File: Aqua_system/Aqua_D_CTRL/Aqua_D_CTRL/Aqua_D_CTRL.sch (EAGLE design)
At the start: 233 parts, among them IC1 SN65HVD3082EDR, IC2 CSTNE8M00G520000R0, IC3 LT6106CS5#TRPBF, IC4 LT6106CS5#TRPBF, IC5 TPS54202DDCR, IC6 LD1117S33TR, IC8 LM317AEMP, J1 ESP32-PICO-KIT, K1 KB20C06A, K2 KB20C06A, Q1 DMP6185SEQ-13, Q10 BC817, Q11 2N7002, Q12 DMP6185SEQ-13, Q13 2N7002, Q14 DMP6185SEQ-13, Q15 2N7002, Q16 DMP6185SEQ-13, Q17 BC817, Q18 BC817, Q19 BC817, Q2 2N7002, Q20 BC817, Q21 BC817, Q22 BC817, Q23 BC817, Q3 DMP6185SEQ-13, Q4 2N7002, Q5 DMP6185SEQ-13, Q6 DMP6185SEQ-13, Q7 2N7002, Q8 DMP6185SEQ-13, Q9 2N7002, SW1 L101011MS02Q, U2 RENESAS_R7FA6M5BG3CFBLQFP_144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, X1 B2B-XH-AM(LF)(SN), X10 726386-2TE_726386-2, X11 282834-2, X12 RJ45-8L-B, X13 MICROMATCH-16, X14 RJ45-8L-B, X2 WF2549-2WS05S0B01, X3 282834-3, X4 282834-3, X5 726386-2TE_726386-2, X6 726386-2TE_726386-2, X7 726386-2TE_726386-2, X8 726386-2TE_726386-2, X9 726386-2TE_726386-2

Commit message: HW00.00 Ongoing
Layout ongoing
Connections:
- removed net N$90: C67.2
- net AI_24V0: now also U2B.P502
- net AI_I_SENSE_CONDUTIV_SENSOR: now also U2B.P503
- net AI_I_SENSE_PH_SENSOR: now also U2B.P500
- net AI_V_CONDUCTIV_SENSOR: now also U2B.P504
- net AI_V_PH_SENSOR: now also U2B.P501
- net GND: now also U2B.AVSS0, U2B.VREFL0, U2B.VSS, U2B.VSS_5, U2B.VSS_6
- net VCC: now also C67.2, U2B.AVCC0, U2B.VCC, U2B.VCC_5, U2B.VCC_6, U2B.VREFH0
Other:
- moved on the sheet: C60, C61, C62, C63, C64, C65, C66, C67, C68

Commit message: HW00.00 Layout Ongoing
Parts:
- removed R95: 2.2K 1%, Labops_Lib_AH:R_0603
- C67: value 100nF/50V -> 1unF/50V
- U2: value RENESAS_R7FA6M5BG3CFBLQFP_144_20X20_REN-M -> R7FA6M5BG3CFBLQFP_144_20X20_REN-M; device 3D_MIG_Controller:RENESAS_R7FA6M5BG3CFBLQFP_144_20X20_REN-M -> Labops_Lib_AH:R7FA6M5BG3CFBLQFP_144_20X20_REN-M
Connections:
- removed net N$59: R95.2
- net GND: now also U2B.VREFL; no longer R95.1, U2B.VREFL0
- net VCC: now also U2B.VREFH; no longer U2B.VREFH0
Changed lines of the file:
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@@
 <part name="C50" library="Labops_Lib_AH" deviceset="C_0603" device="" value="100nF/50V"/>
 <part name="GND70" library="3D_MIG_Controller" deviceset="GND" device=""/>
-<part name="R95" library="Labops_Lib_AH" deviceset="R_0603" device="" value="2.2K 1%"/>
-<part name="GND71" library="3D_MIG_Controller" deviceset="GND" device=""/>
 <part name="GND72" library="3D_MIG_Controller" deviceset="GND" device=""/>
 <part name="C51" library="Labops_Lib_AH" deviceset="C_0603" device="" value="100nF/50V"/>
@@
 <part name="GND94" library="3D_MIG_Controller" deviceset="GND" device=""/>
 <part name="GND95" library="3D_MIG_Controller" deviceset="GND" device=""/>
-<part name="C67" library="Labops_Lib_AH" deviceset="C_0603" device="" value="100nF/50V"/>
+<part name="C67" library="Labops_Lib_AH" deviceset="C_0603" device="" value="1unF/50V"/>
 <part name="C68" library="Labops_Lib_AH" deviceset="C_0603" device="" value="100nF/50V"/>
 <part name="GND97" library="3D_MIG_Controller" deviceset="GND" device=""/>
@@
 <part name="C41" library="Labops_Lib_AH" deviceset="C_0603" device="" value="100nF/50V"/>
 <part name="GND52" library="3D_MIG_Controller" deviceset="GND" device=""/>
-<part name="U2" library="3D_MIG_Controller" deviceset="RENESAS_R7FA6M5BG3CFB" device="LQFP_144_20X20_REN-M"/>
+<part name="U2" library="Labops_Lib_AH" deviceset="R7FA6M5BG3CFB" device="LQFP_144_20X20_REN-M"/>
 <part name="GND53" library="3D_MIG_Controller" deviceset="GND" device=""/>
 <part name="GND54" library="3D_MIG_Controller" deviceset="GND" device=""/>
 <part name="GND55" library="3D_MIG_Controller" deviceset="GND" device=""/>
-<part name="GND56" library="3D_MIG_Controller" deviceset="GND" device=""/>
 <part name="GND57" library="3D_MIG_Controller" deviceset="GND" device=""/>
+<part name="GND58" library="3D_MIG_Controller" deviceset="GND" device=""/>
 </parts>
 <sheets>
@@
 </instance>
 <instance part="GND70" gate="1" x="609.6" y="127.508" smashed="yes"/>
-<instance part="R95" gate="G$1" x="564.896" y="158.242" smashed="yes" rot="R180">
-<attribute name="NAME" x="566.166" y="163.3474" size="1.778" layer="95" rot="R180"/>
-<attribute name="VALUE" x="568.706" y="161.544" size="1.778" layer="96" rot="R180"/>
-</instance>
-<instance part="GND71" gate="1" x="573.278" y="158.242" smashed="yes" rot="R90"/>
 <instance part="GND72" gate="1" x="543.56" y="139.7" smashed="yes"/>
 <instance part="C51" gate="G$1" x="541.782" y="133.096" smashed="yes" rot="R180">
@@
 <instance part="GND90" gate="1" x="187.96" y="172.72" smashed="yes"/>
 <instance part="C61" gate="G$1" x="167.64" y="139.7" smashed="yes" rot="R180">
-<attribute name="NAME" x="169.545" y="133.096" size="1.778" layer="95" rot="R90"/>
-<attribute name="VALUE" x="168.529" y="128.524" size="1.778" layer="96" rot="R270"/>
-</instance>
-<instance part="GND91" gate="1" x="152.4" y="137.16" smashed="yes" rot="R270"/>
+<attribute name="NAME" x="172.085" y="138.176" size="1.778" layer="95" rot="R90"/>
+<attribute name="VALUE" x="173.609" y="143.764" size="1.778" layer="96" rot="R270"/>
+</instance>
+<instance part="GND91" gate="1" x="152.4" y="134.62" smashed="yes" rot="R270"/>
 <instance part="C62" gate="G$1" x="160.02" y="139.7" smashed="yes" rot="R180">
-<attribute name="NAME" x="159.385" y="133.096" size="1.778" layer="95" rot="R90"/>
-<attribute name="VALUE" x="158.369" y="128.524" size="1.778" layer="96" rot="R270"/>
+<attribute name="NAME" x="154.305" y="140.716" size="1.778" layer="95" rot="R90"/>
+<attribute name="VALUE" x="155.829" y="146.304" size="1.778" layer="96" rot="R270"/>
 </instance>
 <instance part="C63" gate="G$1" x="119.38" y="149.86" smashed="yes" rot="R180">
@@
 <instance part="GND54" gate="1" x="269.24" y="116.84" smashed="yes"/>
 <instance part="GND55" gate="1" x="195.58" y="134.62" smashed="yes" rot="R270"/>
-<instance part="GND56" gate="1" x="172.72" y="149.86" smashed="yes"/>
 <instance part="GND57" gate="1" x="180.34" y="149.86" smashed="yes" rot="R270"/>
+<instance part="GND58" gate="1" x="193.04" y="139.7" smashed="yes"/>
 </instances>
 <busses>
@@
 <pinref part="GND70" gate="1" pin="GND"/>
 <wire x1="609.6" y1="141.478" x2="609.6" y2="130.048" width="0.1524" layer="91"/>
-</segment>
-<segment>
-<pinref part="R95" gate="G$1" pin="1"/>
-<pinref part="GND71" gate="1" pin="GND"/>
-<wire x1="569.976" y1="158.242" x2="570.738" y2="158.242" width="0.1524" layer="91"/>
 </segment>
 <segment>
@@
 <pinref part="GND88" gate="1" pin="GND"/>
 <wire x1="274.32" y1="116.84" x2="274.32" y2="114.3" width="0.1524" layer="91"/>
-</segment>
-<segment>
-<pinref part="GND91" gate="1" pin="GND"/>
-<pinref part="C62" gate="G$1" pin="1"/>
-<wire x1="154.94" y1="137.16" x2="160.02" y2="137.16" width="0.1524" layer="91"/>
-<pinref part="C61" gate="G$1" pin="1"/>
-<wire x1="160.02" y1="137.16" x2="167.64" y2="137.16" width="0.1524" layer="91"/>
-<junction x="160.02" y="137.16"/>
 </segment>
 <segment>
@@
 </segment>
 <segment>
-<pinref part="U2" gate="B" pin="VREFL0"/>
-<pinref part="GND56" gate="1" pin="GND"/>
-<wire x1="203.2" y1="152.4" x2="172.72" y2="152.4" width="0.1524" layer="91"/>
+<pinref part="GND91" gate="1" pin="GND"/>
+<pinref part="C62" gate="G$1" pin="1"/>
+<wire x1="154.94" y1="134.62" x2="160.02" y2="134.62" width="0.1524" layer="91"/>
+<wire x1="160.02" y1="134.62" x2="160.02" y2="137.16" width="0.1524" layer="91"/>
+<wire x1="160.02" y1="134.62" x2="167.64" y2="134.62" width="0.1524" layer="91"/>
+<junction x="160.02" y="134.62"/>
+<pinref part="C61" gate="G$1" pin="1"/>
+<wire x1="167.64" y1="134.62" x2="167.64" y2="137.16" width="0.1524" layer="91"/>
+</segment>
+<segment>
+<pinref part="GND58" gate="1" pin="GND"/>
+<pinref part="U2" gate="B" pin="VREFL"/>
+<wire x1="193.04" y1="142.24" x2="203.2" y2="142.24" width="0.1524" layer="91"/>
 </segment>
 </net>
@@
 <wire x1="109.22" y1="153.416" x2="109.22" y2="154.94" width="0.1524" layer="91"/>
 <junction x="109.22" y="154.94"/>
-<pinref part="U2" gate="B" pin="VREFH0"/>
-<wire x1="119.38" y1="154.94" x2="203.2" y2="154.94" width="0.1524" layer="91"/>
+<wire x1="119.38" y1="154.94" x2="193.04" y2="154.94" width="0.1524" layer="91"/>
 <junction x="119.38" y="154.94"/>
+<wire x1="193.04" y1="154.94" x2="193.04" y2="144.78" width="0.1524" layer="91"/>
+<pinref part="U2" gate="B" pin="VREFH"/>
+<wire x1="193.04" y1="144.78" x2="203.2" y2="144.78" width="0.1524" layer="91"/>
 </segment>
 <segment>
@@
 <segment>
 <pinref part="C68" gate="G$1" pin="2"/>
-<label x="137.16" y="132.08" size="1.778" layer="95" rot="R180" xref="yes"/>
-<wire x1="137.16" y1="132.08" x2="147.32" y2="132.08" width="0.1524" layer="91"/>
+<label x="114.3" y="132.08" size="1.778" layer="95" rot="R180" xref="yes"/>
+<wire x1="114.3" y1="132.08" x2="147.32" y2="132.08" width="0.1524" layer="91"/>
 <wire x1="147.32" y1="132.08" x2="147.32" y2="130.556" width="0.1524" layer="91"/>
 <wire x1="147.32" y1="132.08" x2="203.2" y2="132.08" width="0.1524" layer="91"/>
@@
 </segment>
 </net>
-<net name="N$59" class="3">
-<segment>
-<pinref part="R95" gate="G$1" pin="2"/>
-<wire x1="559.816" y1="158.242" x2="557.28" y2="158.242" width="0.1524" layer="91"/>
-<wire x1="557.28" y1="158.242" x2="557.28" y2="158.28" width="0.1524" layer="91"/>
-</segment>
-</net>

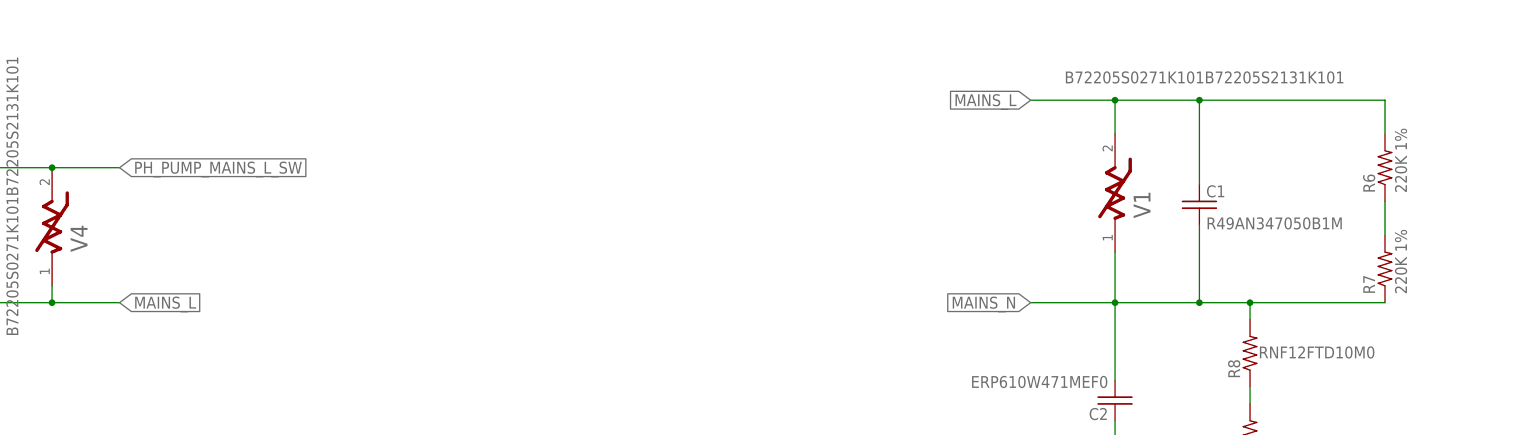
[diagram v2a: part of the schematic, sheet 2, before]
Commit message: HW00.00 Ongoing
Layout Copper Pouring
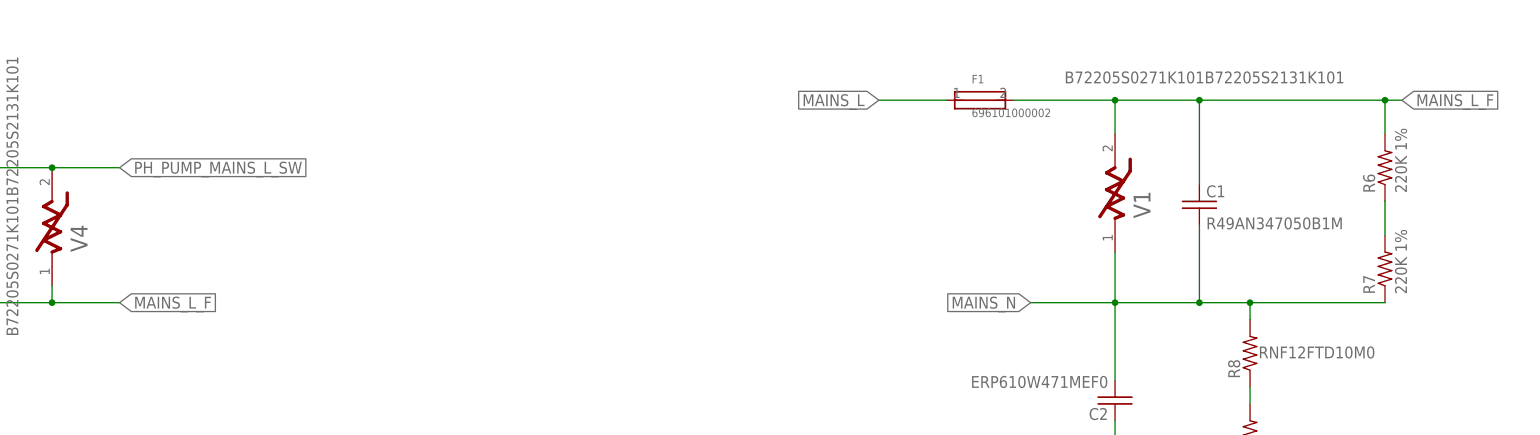
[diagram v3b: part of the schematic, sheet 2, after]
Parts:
- added F1: 696101000002, Labops_Lib_AH:696101000002
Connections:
- new net MAINS_L_F: C1.1, F1.P$2, K1.4, K2.4, R6.2, V1.2, V4.1, V5.1
- net MAINS_L: now also F1.P$1; no longer C1.1, K1.4, K2.4, R6.2, V1.2, V4.1, V5.1
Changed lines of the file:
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@@
 <part name="GND57" library="3D_MIG_Controller" deviceset="GND" device=""/>
 <part name="GND58" library="3D_MIG_Controller" deviceset="GND" device=""/>
+<part name="F1" library="Labops_Lib_AH" deviceset="696101000002" device=""/>
 </parts>
 <sheets>
@@
 <attribute name="VALUE" x="341.122" y="217.17" size="1.778" layer="96" rot="R90"/>
 </instance>
+<instance part="F1" gate="G$1" x="276.86" y="246.38" smashed="yes">
+<attribute name="NAME" x="275.59" y="248.92" size="1.27" layer="95"/>
+<attribute name="VALUE" x="275.59" y="243.84" size="1.27" layer="96"/>
+</instance>
 </instances>
 <busses>
@@
 </segment>
 </net>
-<net name="MAINS_L" class="4">
+<net name="MAINS_L_F" class="4">
 <segment>
 <wire x1="337.82" y1="246.38" x2="309.88" y2="246.38" width="0.1524" layer="91"/>
-<label x="284.48" y="246.38" size="1.778" layer="95" rot="R180" xref="yes"/>
 <pinref part="C1" gate="G$1" pin="1"/>
 <wire x1="309.88" y1="233.68" x2="309.88" y2="246.38" width="0.1524" layer="91"/>
@@
 <pinref part="V1" gate="G$1" pin="2"/>
 <wire x1="297.18" y1="241.3" x2="297.18" y2="246.38" width="0.1524" layer="91"/>
-<wire x1="284.48" y1="246.38" x2="297.18" y2="246.38" width="0.1524" layer="91"/>
 <wire x1="309.88" y1="246.38" x2="297.18" y2="246.38" width="0.1524" layer="91"/>
 <junction x="309.88" y="246.38"/>
 <junction x="297.18" y="246.38"/>
 <pinref part="R6" gate="G$1" pin="2"/>
+<wire x1="281.94" y1="246.38" x2="297.18" y2="246.38" width="0.1524" layer="91"/>
+<pinref part="F1" gate="G$1" pin="P$2"/>
+<label x="340.36" y="246.38" size="1.778" layer="95" xref="yes"/>
+<wire x1="337.82" y1="246.38" x2="340.36" y2="246.38" width="0.1524" layer="91"/>
+<junction x="337.82" y="246.38"/>
 </segment>
 <segment>
@@
 </segment>
 </net>
+<net name="MAINS_L" class="4">
+<segment>
+<pinref part="F1" gate="G$1" pin="P$1"/>
+<wire x1="271.78" y1="246.38" x2="261.62" y2="246.38" width="0.1524" layer="91"/>
+<label x="261.62" y="246.38" size="1.778" layer="95" rot="R180" xref="yes"/>
+</segment>
+</net>
 </nets>
 </sheet>
@@
 </segment>
 </net>
-<net name="MAINS_L" class="4">
+<net name="MAINS_L_F" class="4">
 <segment>
 <pinref part="K2" gate="G$1" pin="4"/>
@@
 <wire x1="17.78" y1="132.08" x2="27.94" y2="132.08" width="0.1524" layer="91"/>
 <label x="27.94" y="132.08" size="1.778" layer="95" xref="yes"/>
-</segment>
-</net>
-<net name="MAINS_L" class="4">
-<segment>
-<pinref part="X10" gate="G$0" pin="1"/>
-<wire x1="17.78" y1="114.3" x2="27.94" y2="114.3" width="0.1524" layer="91"/>
-<label x="27.94" y="114.3" size="1.778" layer="95" xref="yes"/>
 </segment>
 </net>
@@
 </segment>
 </net>
+<net name="MAINS_L" class="4">
+<segment>
+<pinref part="X10" gate="G$0" pin="1"/>
+<wire x1="17.78" y1="114.3" x2="27.94" y2="114.3" width="0.1524" layer="91"/>
+<label x="27.94" y="114.3" size="1.778" layer="95" xref="yes"/>
+</segment>
+</net>

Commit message: HW00.00 Ongoing
Finalizing Layout
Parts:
- R42: value 10K 1% -> 100R 1%
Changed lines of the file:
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@@
 <setting verticaltext="up"/>
 </settings>
-<grid distance="0.1" unitdist="inch" unit="inch" style="lines" multiple="1" display="yes" altdistance="0.01" altunitdist="inch" altunit="inch"/>
+<grid distance="0.1" unitdist="inch" unit="inch" style="lines" multiple="1" display="no" altdistance="0.01" altunitdist="inch" altunit="inch"/>
 <layers>
 <layer number="1" name="Top" color="4" fill="1" visible="no" active="no"/>
@@
 <part name="R40" library="Labops_Lib_AH" deviceset="R_0603" device="" value="22K 1%"/>
 <part name="R41" library="Labops_Lib_AH" deviceset="R_0603" device="" value="2.8K 1%"/>
-<part name="R42" library="Labops_Lib_AH" deviceset="R_0603" device="" value="10K 1%"/>
+<part name="R42" library="Labops_Lib_AH" deviceset="R_0603" device="" value="100R 1%"/>
 <part name="D10" library="Labops_Lib_AH" deviceset="BAS40-04,215" device=""/>
 <part name="P+8" library="supply1" library_urn="urn:adsk.eagle:library:371" deviceset="VCC" device="" value="3V3"/>
@@
 </segment>
 </net>
-<net name="DO_PH_SENSOR_ON" class="3">
-<segment>
-<label x="276.86" y="99.06" size="1.778" layer="95" rot="MR270" xref="yes"/>
-<pinref part="U2" gate="B" pin="P101"/>
-<wire x1="264.16" y1="104.14" x2="276.86" y2="104.14" width="0.1524" layer="91"/>
-<wire x1="276.86" y1="104.14" x2="276.86" y2="99.06" width="0.1524" layer="91"/>
-</segment>
-</net>
 <net name="AI_V_PH_SENSOR" class="3">
 <segment>
@@
 <pinref part="U2" gate="B" pin="P100"/>
 <wire x1="264.16" y1="101.6" x2="269.24" y2="101.6" width="0.1524" layer="91"/>
-<wire x1="269.24" y1="101.6" x2="269.24" y2="93.98" width="0.1524" layer="91"/>
-<label x="269.24" y="93.98" size="1.778" layer="95" rot="R270" xref="yes"/>
+<wire x1="269.24" y1="101.6" x2="269.24" y2="96.52" width="0.1524" layer="91"/>
+<label x="269.24" y="96.52" size="1.778" layer="95" rot="R270" xref="yes"/>
+</segment>
+</net>
+<net name="DO_PH_SENSOR_ON" class="3">
+<segment>
+<pinref part="U2" gate="B" pin="P101"/>
+<wire x1="264.16" y1="104.14" x2="274.32" y2="104.14" width="0.1524" layer="91"/>
+<wire x1="274.32" y1="104.14" x2="274.32" y2="96.52" width="0.1524" layer="91"/>
+<label x="274.32" y="96.52" size="1.778" layer="95" rot="R270" xref="yes"/>
 </segment>
 </net>

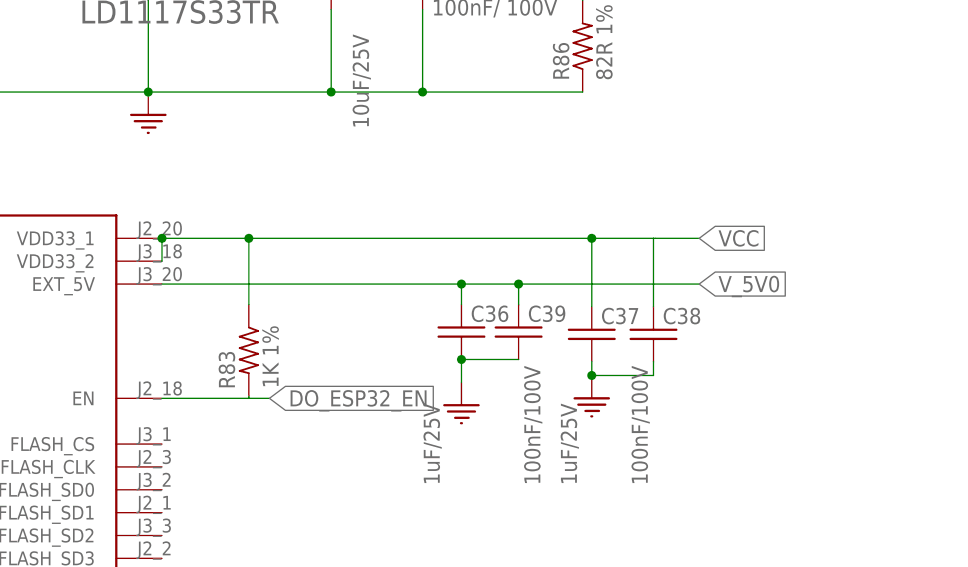
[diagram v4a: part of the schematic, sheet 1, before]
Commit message: HW00.00 Ongoing
Added an assembly variant Rseries between ESP32 5V supply pin and 5V0 Rail
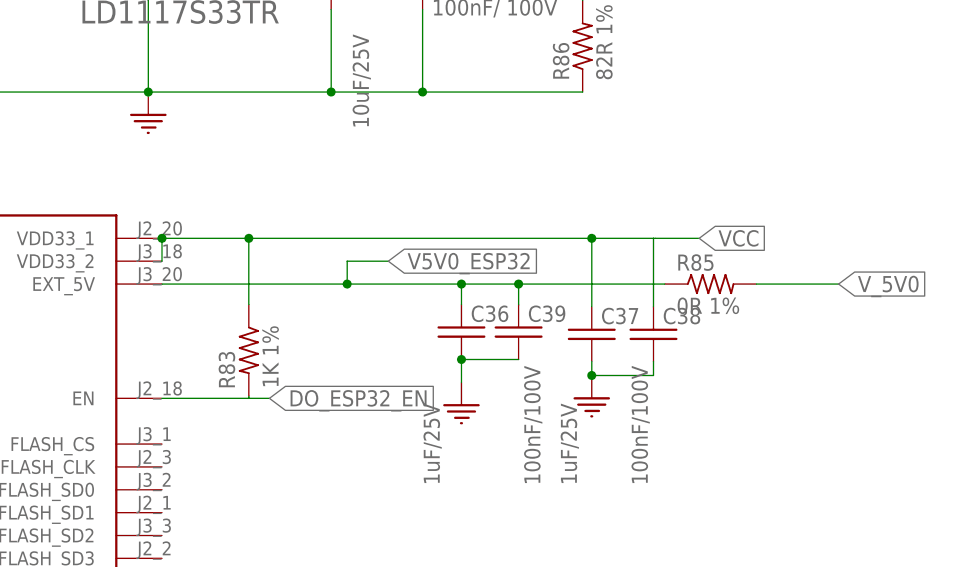
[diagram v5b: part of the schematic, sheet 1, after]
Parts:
- added R85: 0R 1%, Labops_Lib_AH:R_1206
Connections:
- new net V5V0_ESP32: C36.1, C39.1, J1.EXT_5V, R85.1
- net V_5V0: now also R85.2; no longer C36.1, C39.1, J1.EXT_5V
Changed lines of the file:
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@@
 <setting verticaltext="up"/>
 </settings>
-<grid distance="0.1" unitdist="inch" unit="inch" style="lines" multiple="1" display="no" altdistance="0.01" altunitdist="inch" altunit="inch"/>
+<grid distance="0.01" unitdist="inch" unit="inch" style="lines" multiple="1" display="yes" altdistance="0.01" altunitdist="inch" altunit="inch"/>
 <layers>
 <layer number="1" name="Top" color="4" fill="1" visible="no" active="no"/>
@@
 <part name="GND58" library="3D_MIG_Controller" deviceset="GND" device=""/>
 <part name="F1" library="Labops_Lib_AH" deviceset="696101000002" device=""/>
+<part name="R85" library="Labops_Lib_AH" deviceset="R_1206" device="" value="0R 1%"/>
 </parts>
 <sheets>
@@
 <attribute name="NAME" x="334.264" y="177.673" size="1.778" layer="95"/>
 <attribute name="VALUE" x="335.661" y="159.512" size="1.778" layer="96" rot="R90"/>
+</instance>
+<instance part="R85" gate="G$1" x="354.584" y="181.864" smashed="yes">
+<attribute name="NAME" x="350.774" y="183.3626" size="1.778" layer="95"/>
+<attribute name="VALUE" x="350.774" y="178.562" size="1.778" layer="96"/>
 </instance>
 </instances>
@@
 </segment>
 <segment>
-<pinref part="J1" gate="G$1" pin="EXT_5V"/>
-<wire x1="293.624" y1="181.864" x2="326.898" y2="181.864" width="0.1524" layer="91"/>
-<label x="353.314" y="181.864" size="1.778" layer="95" xref="yes"/>
-<pinref part="C36" gate="G$1" pin="1"/>
-<wire x1="326.898" y1="181.864" x2="333.248" y2="181.864" width="0.1524" layer="91"/>
-<wire x1="333.248" y1="181.864" x2="353.314" y2="181.864" width="0.1524" layer="91"/>
-<wire x1="326.898" y1="179.578" x2="326.898" y2="181.864" width="0.1524" layer="91"/>
-<junction x="326.898" y="181.864"/>
-<pinref part="C39" gate="G$1" pin="1"/>
-<wire x1="333.248" y1="179.578" x2="333.248" y2="181.864" width="0.1524" layer="91"/>
-<junction x="333.248" y="181.864"/>
+<pinref part="R85" gate="G$1" pin="2"/>
+<wire x1="359.664" y1="181.864" x2="368.808" y2="181.864" width="0.1524" layer="91"/>
+<label x="368.808" y="181.864" size="1.778" layer="95" xref="yes"/>
 </segment>
 </net>
@@
 </segment>
 </net>
+<net name="V5V0_ESP32" class="0">
+<segment>
+<pinref part="R85" gate="G$1" pin="1"/>
+<pinref part="C39" gate="G$1" pin="1"/>
+<wire x1="349.504" y1="181.864" x2="333.248" y2="181.864" width="0.1524" layer="91"/>
+<wire x1="333.248" y1="181.864" x2="333.248" y2="179.578" width="0.1524" layer="91"/>
+<pinref part="C36" gate="G$1" pin="1"/>
+<pinref part="J1" gate="G$1" pin="EXT_5V"/>
+<wire x1="314.198" y1="181.864" x2="293.624" y2="181.864" width="0.1524" layer="91"/>
+<wire x1="333.248" y1="181.864" x2="326.898" y2="181.864" width="0.1524" layer="91"/>
+<junction x="333.248" y="181.864"/>
+<junction x="314.198" y="181.864"/>
+<label x="318.77" y="184.404" size="1.778" layer="95" xref="yes"/>
+<wire x1="326.898" y1="181.864" x2="314.198" y2="181.864" width="0.1524" layer="91"/>
+<wire x1="318.77" y1="184.404" x2="314.198" y2="184.404" width="0.1524" layer="91"/>
+<wire x1="314.198" y1="184.404" x2="314.198" y2="181.864" width="0.1524" layer="91"/>
+<wire x1="326.898" y1="179.578" x2="326.898" y2="181.864" width="0.1524" layer="91"/>
+<junction x="326.898" y="181.864"/>
+</segment>
+</net>
